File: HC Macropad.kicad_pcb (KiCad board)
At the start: 2 copper layers, 173.2 x 57 mm, 65 parts, among them J1 USB_C_Receptacle_USB2.0_16P, J2 Conn_01x02_Socket, J3 Conn_01x04_Socket, J4 Conn_01x04_Socket, J5 Conn_01x04_Socket, SW1 SW_Push, U1 RP2040, U2 W25Q128JVPIQ, U3 AP2127K-3.3, U4 USBLC6-2P6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

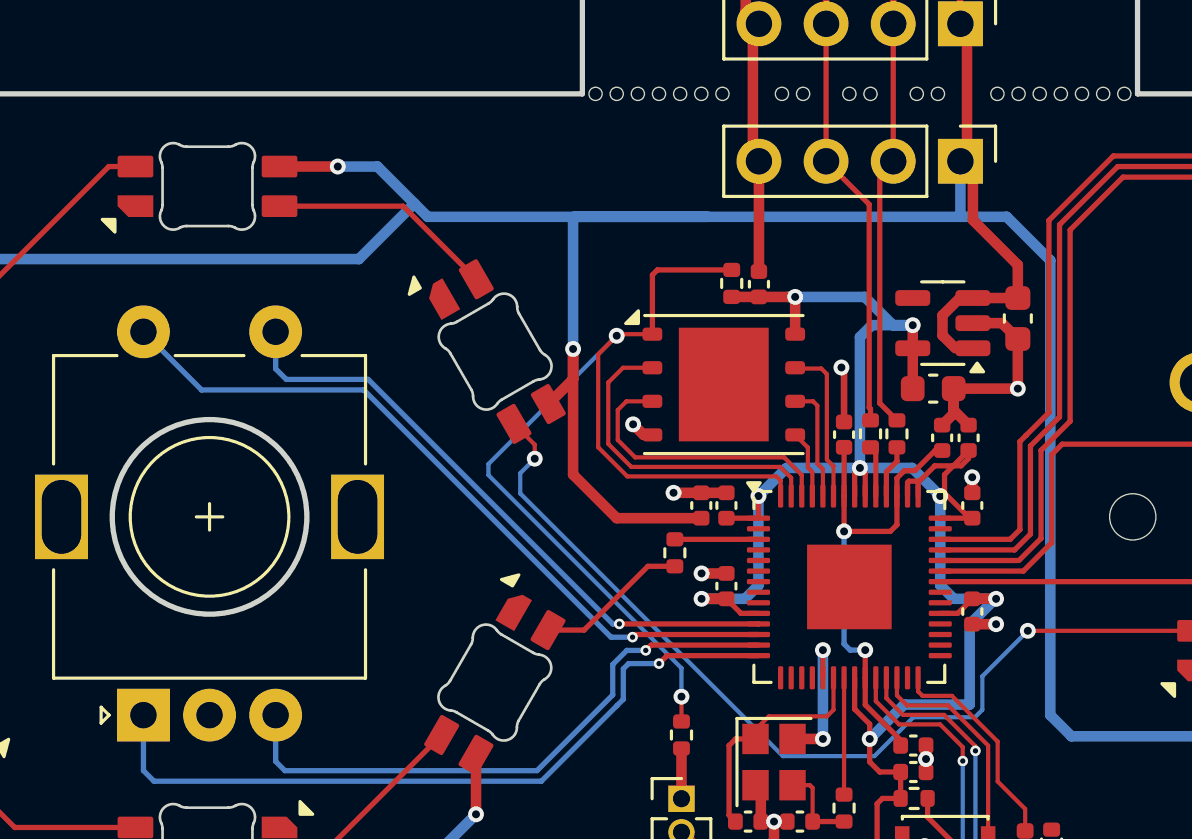
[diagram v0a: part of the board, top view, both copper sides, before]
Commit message: Minor routing changes
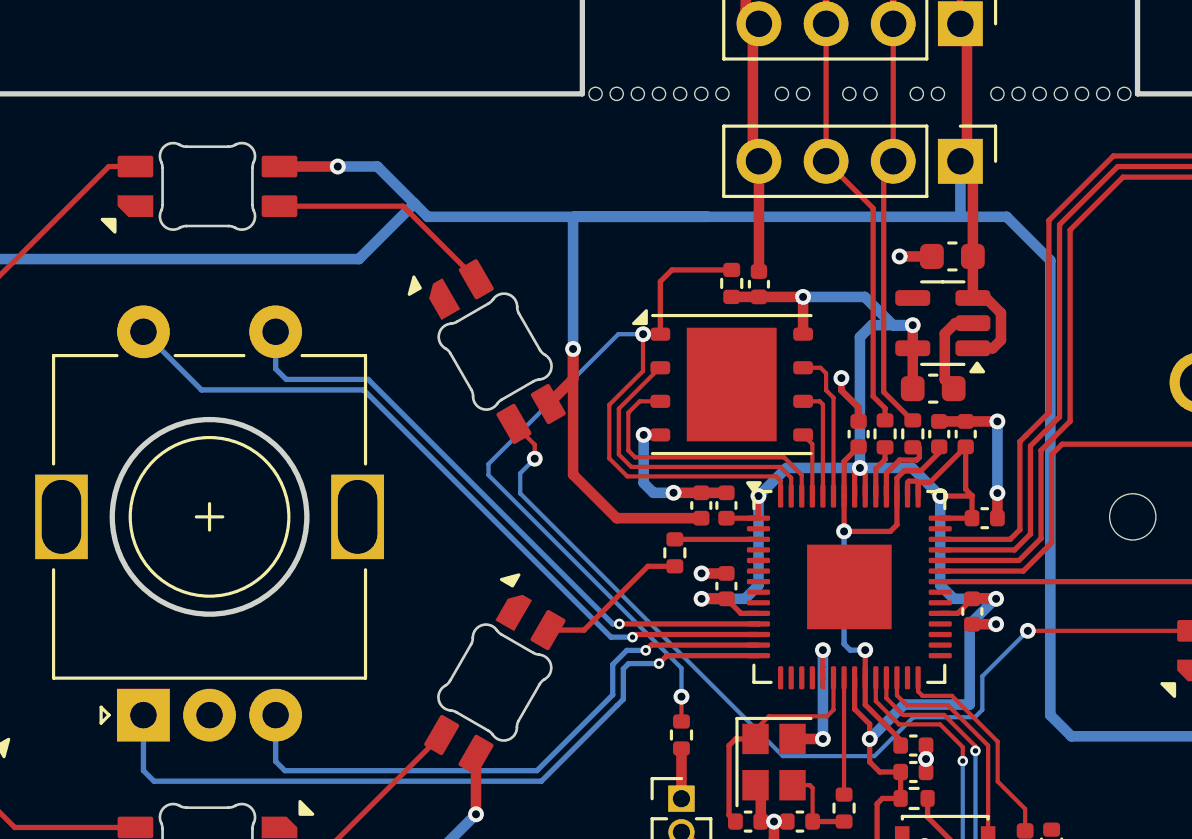
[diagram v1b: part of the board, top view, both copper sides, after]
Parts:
- moved C1 3.41 mm to (123.2, 82.9), turned to 180 degrees
- moved C11 0.67 mm to (124.5, 92.8), turned to 0 degrees
- moved R7 0.60 mm to (121.8, 89.6)
- moved C7 0.55 mm to (119.7, 89.6)
- moved R6 0.55 mm to (120.7, 89.6)
- moved U2 0.30 mm to (114.9, 87.7)
- moved C5 0.18 mm to (123.8, 89.6)
- moved C6 0.18 mm to (122.8, 89.6)
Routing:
- net GND: track 53.9 -> 56.9 mm, vias 17 -> 18
- net +5V: track 316.2 -> 314.9 mm
- net /MCU/QSPI_D1: track 12.4 -> 11.5 mm
- net Net-(U1-USB_DM): track 2.01 -> 2.74 mm
- net /MCU/QSPI_D2: track 10.9 -> 10.3 mm
- net /MCU/QSPI_D3: track 6.30 -> 5.72 mm
- net +1V1: track 18.3 -> 18.8 mm

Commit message: Minor changes before production
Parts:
- R_RGB1: value 330 -> 1k
- moved D1 6.82 mm to (124.0, 98.6), turned to -90 degrees
- moved R1 6.78 mm to (125.0, 98.6), turned to -90 degrees
- moved R2 6.33 mm to (126.0, 98.6), turned to -90 degrees
- moved SW1 3.14 mm to (124.3, 102.3), turned to 90 degrees
- moved J2 2.23 mm to (113.3, 101.2)
- moved R3 1.95 mm to (113.8, 99.2), turned to 0 degrees
- moved R_RGB1 1.53 mm to (114.2, 93.8), turned to 180 degrees
- moved C9 0.78 mm to (114.3, 94.7), turned to 180 degrees
- moved C14 0.54 mm to (121.2, 102.4)
- moved C8 0.54 mm to (121.2, 101.4)
- moved FB1 0.51 mm to (115.9, 68.8)
- moved C13 0.48 mm to (124.5, 96.4), turned to 0 degrees
- moved C5 0.30 mm to (123.5, 89.6)
- moved C6 0.30 mm to (122.5, 89.6)
- moved R7 0.30 mm to (121.5, 89.6)
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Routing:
- net GND: track 56.9 -> 23.5 mm, vias 18 -> 17
- net /MCU/LED: track 8.12 -> 2.15 mm
- net /MCU/SWD: track 41.0 -> 36.0 mm
- net /MCU/~{RESET}: track 12.2 -> 7.31 mm
- net /MCU/SWCLK: track 42.7 -> 39.0 mm
- net +3V3: track 99.7 -> 96.2 mm
- net /MCU/QSPI_~{CS}: track 38.8 -> 35.9 mm
- net RGB: track 3.16 -> 1.22 mm
- net VBUS: track 10.2 -> 12.1 mm
- net Net-(LED0-DIN): track 5.80 -> 7.14 mm
- net /MCU/QSPI_D2: track 10.3 -> 9.20 mm
- net /MCU/QSPI_D1: track 11.5 -> 10.7 mm
- net Net-(C4-Pad1): track 3.27 -> 2.65 mm
- net Net-(U1-USB_DM): track 2.74 -> 2.13 mm
- net Net-(J2-Pin_1): track 1.90 -> 2.40 mm
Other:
- outline, holes or cut-outs redrawn

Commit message: v0.1.3: UFE edition
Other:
- outline, holes or cut-outs redrawn
- board text added: "In memory of the UFE team, it was fun while it lasted!"

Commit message: v0.1.4: HC edition
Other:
- board text removed: "In memory of the UFE team, it was fun while it lasted!"

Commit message: v0.1.5: finalized HC edition
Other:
- board text added: "Happy Contributors"
